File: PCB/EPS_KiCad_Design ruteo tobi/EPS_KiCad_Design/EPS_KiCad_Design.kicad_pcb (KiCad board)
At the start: 4 copper layers, 90 x 90.2 mm, 133 parts, among them IC1 INA226AIDGST, IC10 TPS2553QDBVRQ1, IC11 INA226AIDGST, IC2 TPS2553QDBVRQ1, IC3 INA226AIDGST, IC4 TPS2553QDBVRQ1, IC5 AP63205WU-7, IC6 STM32L433CBT7, IC7 LT3652IMSE#PBF, IC8 INA226AIDGST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

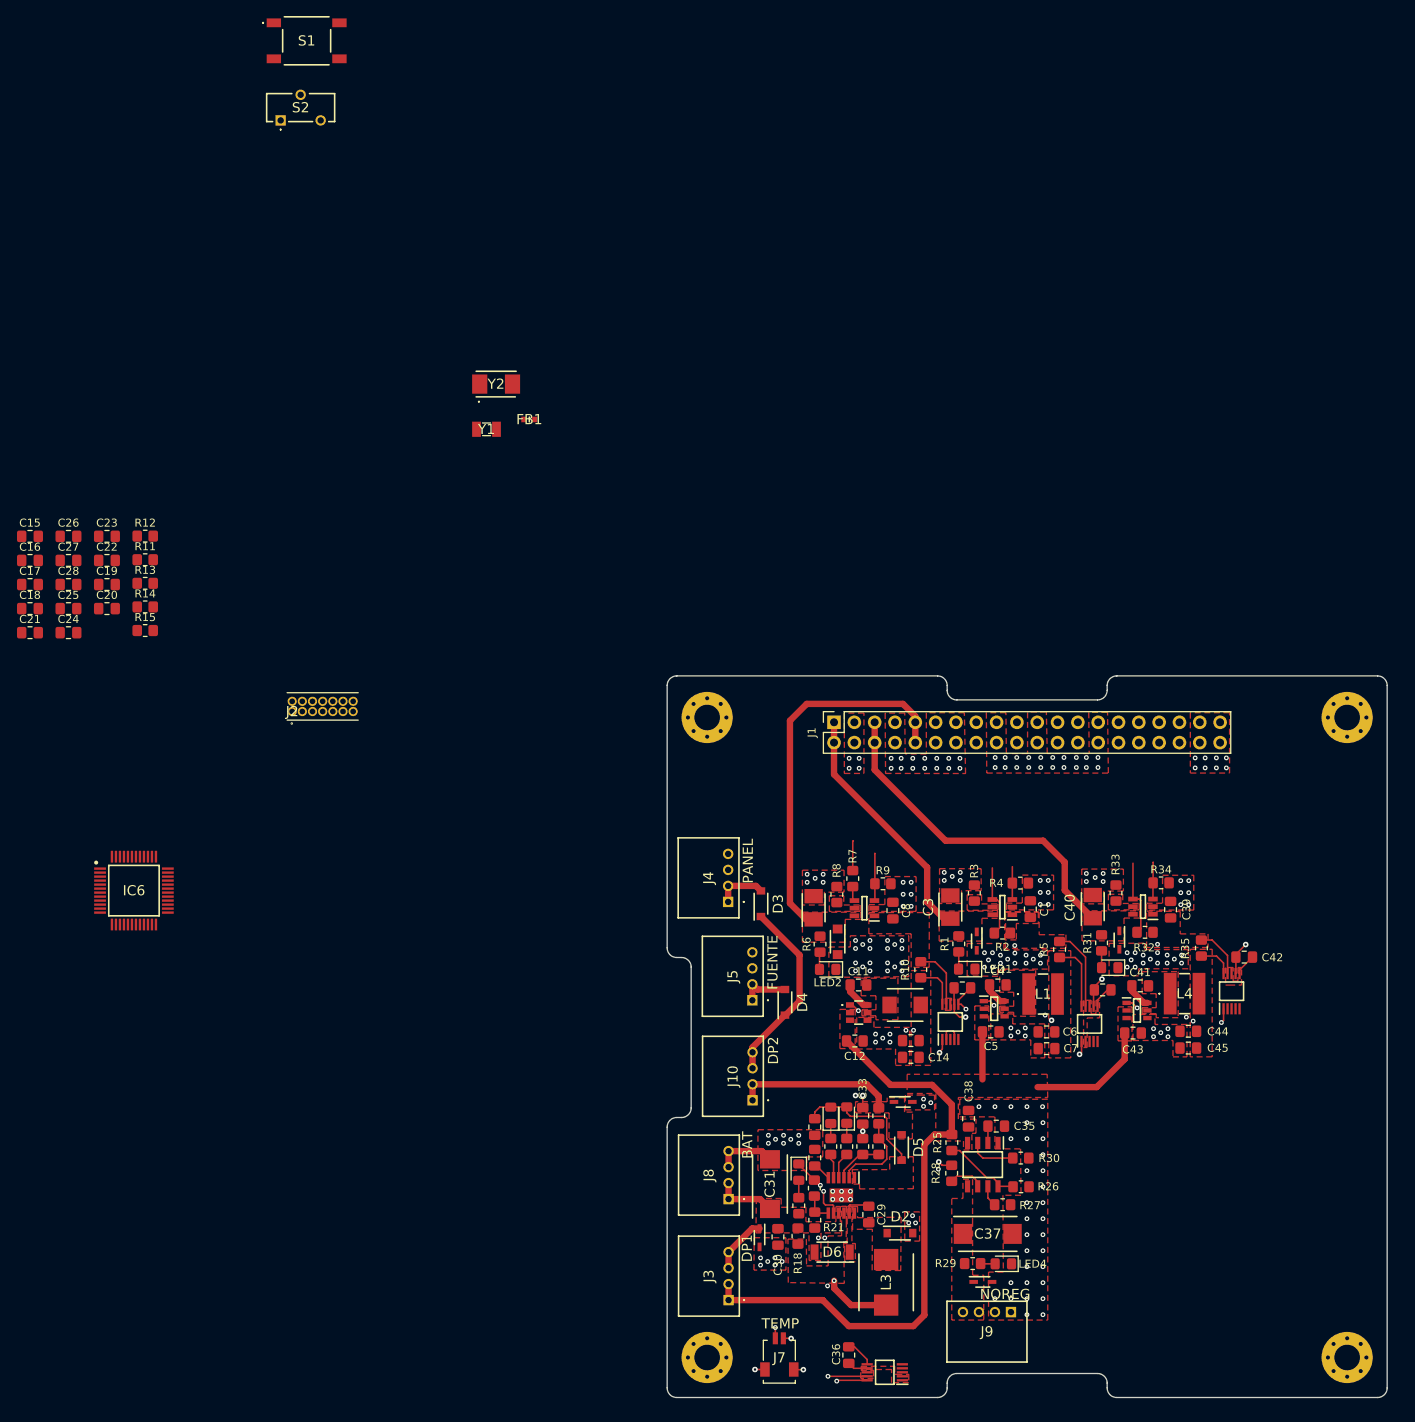
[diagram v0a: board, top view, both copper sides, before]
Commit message: Ruteo parcial de MCU
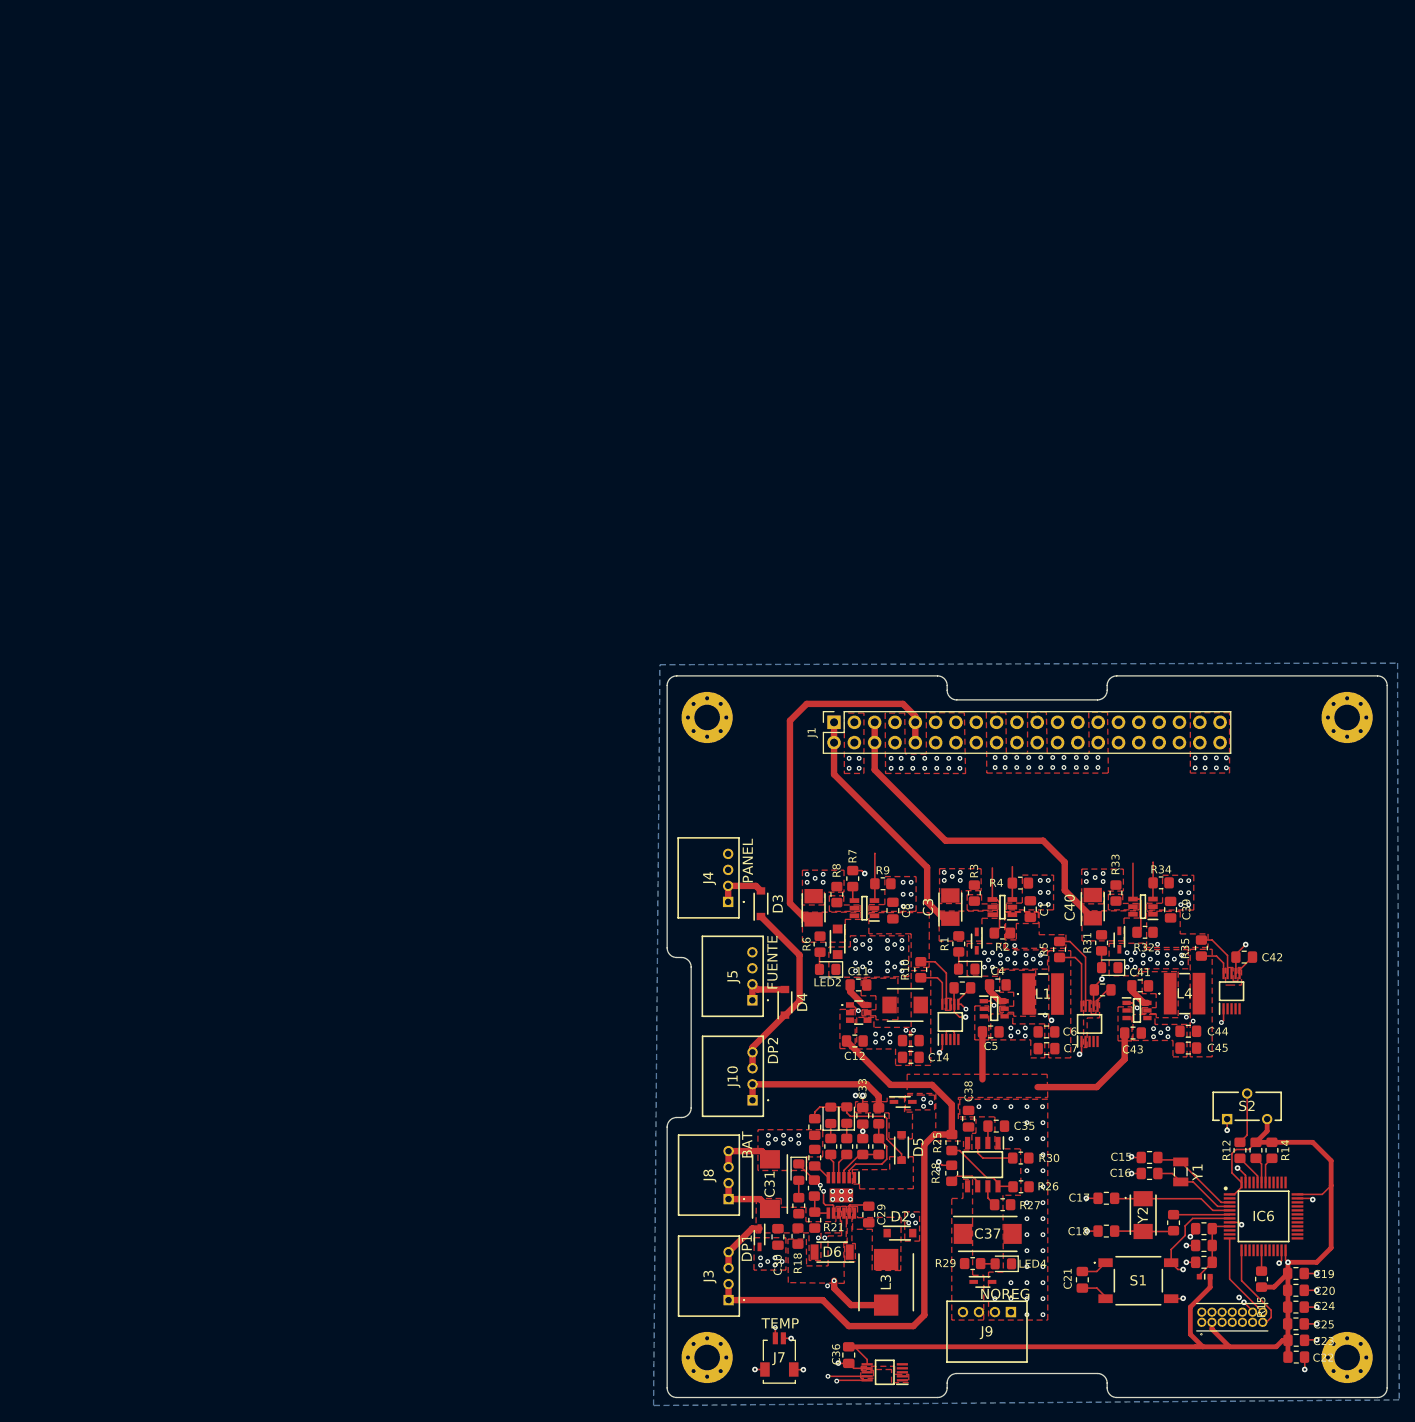
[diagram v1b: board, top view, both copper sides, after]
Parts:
- moved S1 186.6 mm to (158.9, 128.3)
- moved C23 179.4 mm to (178.6, 135.8)
- moved C22 178.9 mm to (178.6, 137.8)
- moved C25 177.6 mm to (178.6, 133.7)
- moved C24 175.1 mm to (178.6, 131.6)
- moved S2 172.0 mm to (170.0, 108.1)
- moved C19 171.8 mm to (178.6, 127.4)
- moved C20 171.3 mm to (178.6, 129.5)
- moved C27 166.9 mm to (167.1, 126.0), turned to 180 degrees
- moved C26 166.2 mm to (167.1, 121.8), turned to 180 degrees
- moved C28 164.2 mm to (167.1, 123.9), turned to 180 degrees
- moved R15 161.4 mm to (174.3, 128.1), turned to 90 degrees
- moved C15 160.0 mm to (160.3, 112.9)
- moved C16 159.6 mm to (160.3, 114.9)
- moved R12 156.9 mm to (171.6, 112.0), turned to 90 degrees
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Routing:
- net 3V3_1: track 52.8 -> 185.6 mm, vias 2 -> 3
- net GND: track 36.2 -> 66.4 mm, vias 221 -> 242
- net /MCU/NRST: track 0.00 -> 24.1 mm, vias 0 -> 2
- net /MCU/PH0: track 0.00 -> 15.1 mm
- net /MCU/PC14: track 0.00 -> 11.4 mm
- net /MCU/PA3: track 0.00 -> 11.2 mm
- net /MCU/PA2: track 0.00 -> 10.9 mm
- net /MCU/PC15: track 0.00 -> 10.7 mm
- net /MCU/VDDA/VREF+: track 0.00 -> 10.0 mm
- net Net-(C18-Pad1): track 0.00 -> 7.46 mm
- net /MCU/PH1: track 0.00 -> 7.20 mm
- net Net-(S2-COM): track 0.00 -> 6.47 mm
- net /MCU/PH3: track 0.00 -> 3.94 mm
- net Net-(S1-N.O._1): track 0.00 -> 3.90 mm
- net Net-(S1-COM_1): track 0.00 -> 3.66 mm
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- added copper zone on B.Cu, net GND

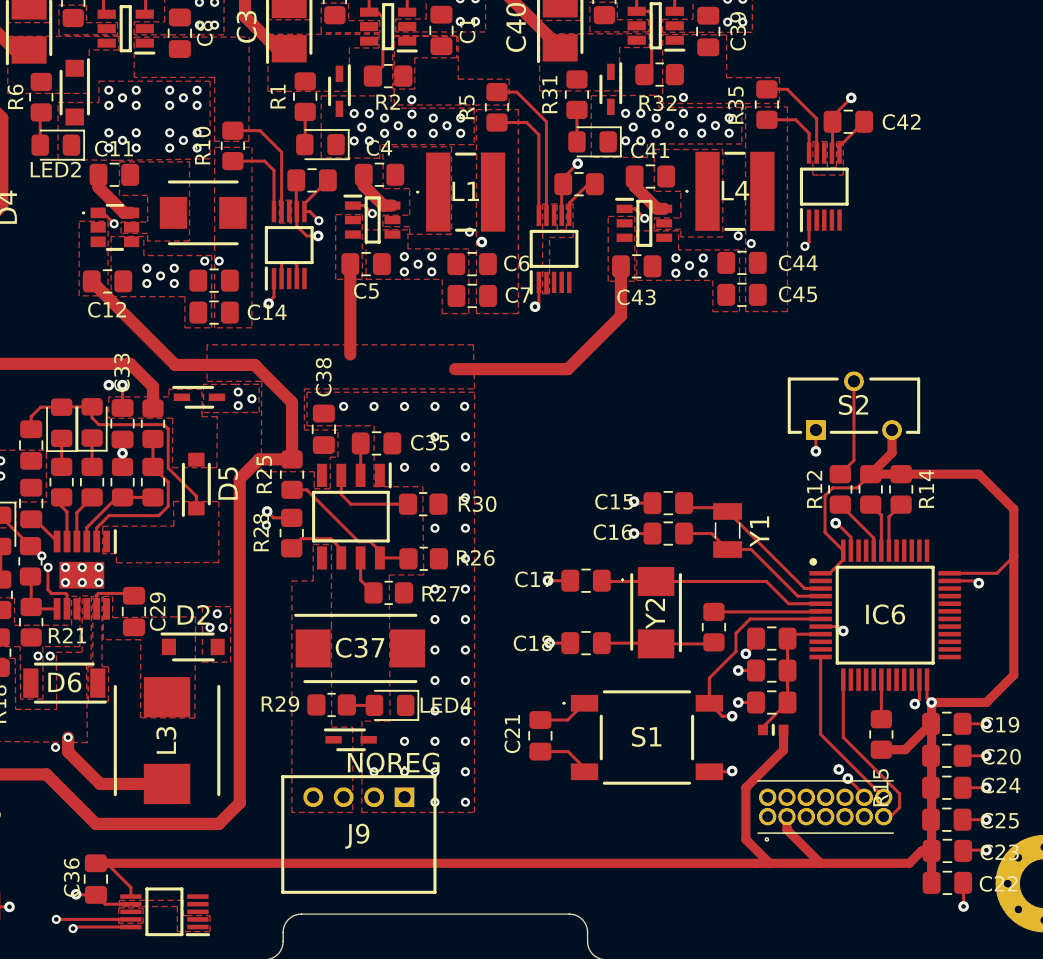
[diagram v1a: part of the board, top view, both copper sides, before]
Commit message: Agregue cosas al ruteo MCU
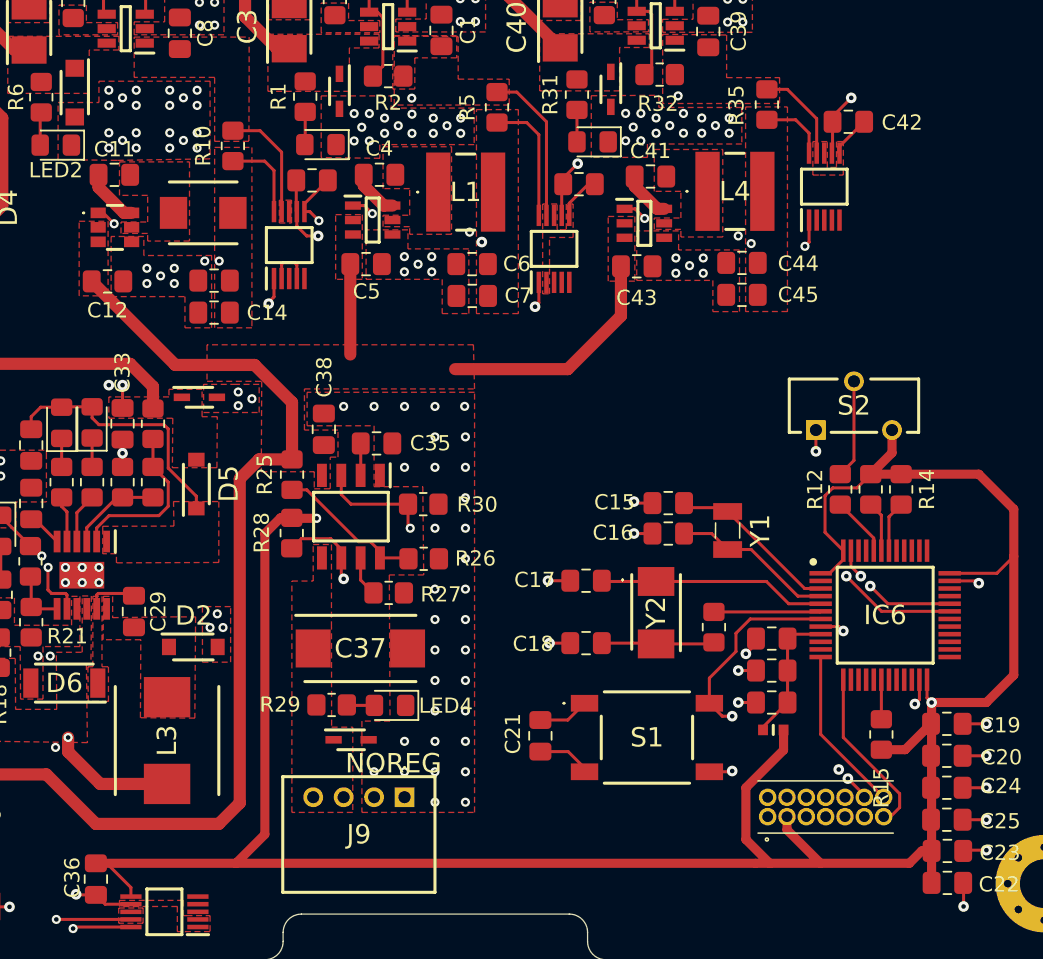
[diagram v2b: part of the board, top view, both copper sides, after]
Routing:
- net GPIO8: track 4.37 -> 46.7 mm, vias 0 -> 2
- net GPIO7: track 5.90 -> 45.2 mm, vias 0 -> 2
- net 3V3_2: track 41.9 -> 68.4 mm
- net 3V3_1: track 185.6 -> 209.7 mm
- net GND: track 66.4 -> 66.0 mm, vias 242 -> 241
